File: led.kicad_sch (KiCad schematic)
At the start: 0 parts

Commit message: Add uC and PWM control for LEDs
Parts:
- added Q2, Q3, Q4, Q5, Q6, Q7: BSS214NW, Package_TO_SOT_SMD:SOT-323_SC-70, symbol Transistor_FET:BSS214NW
- added U10: ATtiny24-20P, Package_DIP:DIP-14_W7.62mm, symbol MCU_Microchip_ATtiny:ATtiny24-20P
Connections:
- new net: Q4.1 (G), U10.10 (PA3)
- new net: Q7.1 (G), U10.13 (AREF/PA0)
- new net: Q6.1 (G), U10.9 (PA4)
- new net: Q2.1 (G), U10.12 (PA1)
- new net: Q3.1 (G), U10.11 (PA2)
- new net: Q5.1 (G), U10.8 (PA5)
- new net GND: Q2.2 (S), Q3.2 (S), Q4.2 (S), Q5.2 (S), Q6.2 (S), Q7.2 (S), U10.14 (GND)
- new net LED_CH1: Q7.3 (D)
- new net LED_CH2: Q2.3 (D)
- new net LED_CH3: Q3.3 (D)
- new net LED_CH4: Q4.3 (D)
- new net LED_CH5: Q6.3 (D)
- new net LED_CH6: Q5.3 (D)
- new net VDD: U10.1 (VCC)

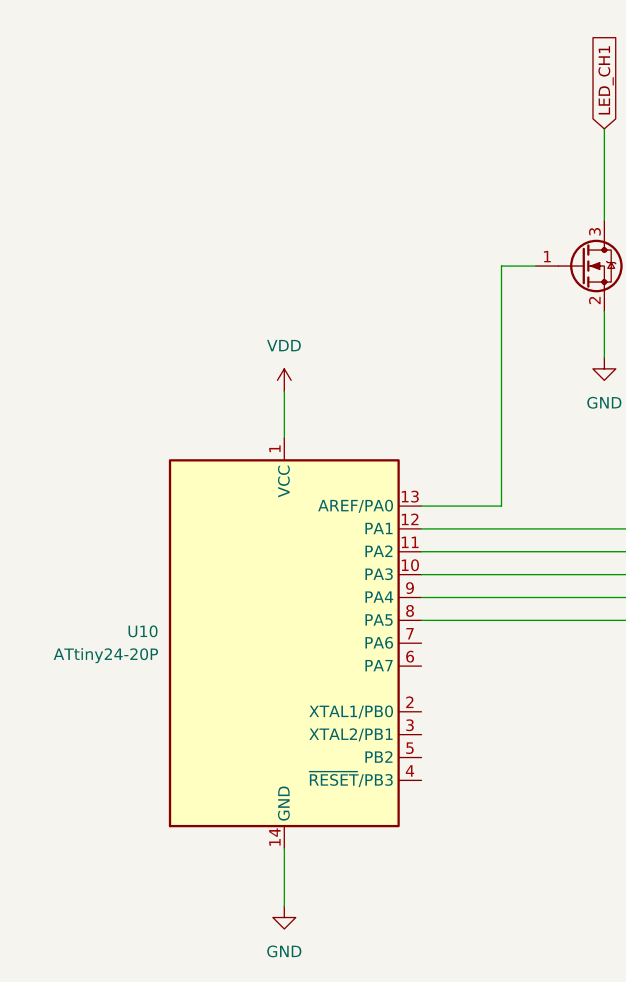
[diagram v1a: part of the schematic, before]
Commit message: Connect uC with LEDs
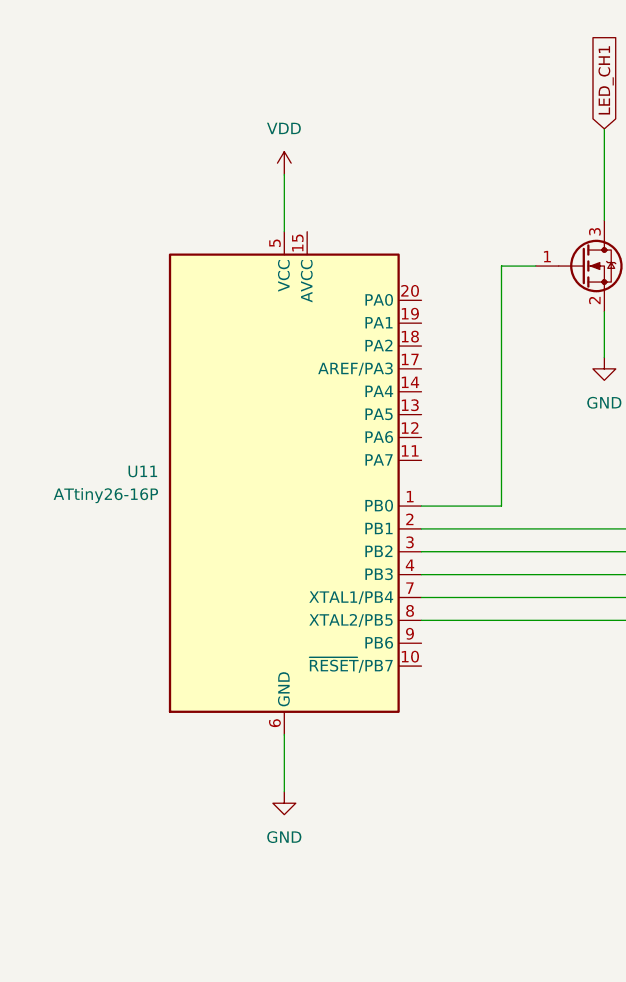
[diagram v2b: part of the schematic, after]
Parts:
- removed U10: ATtiny24-20P, Package_DIP:DIP-14_W7.62mm, symbol MCU_Microchip_ATtiny:ATtiny24-20P
- added U11: ATtiny26-16P, Package_DIP:DIP-20_W7.62mm, symbol MCU_Microchip_ATtiny:ATtiny26-16P
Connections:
- net GND: now also U11.16 (GND), U11.6 (GND)
- net VDD: now also U11.5 (VCC)
- net at Q4.1 (G): now also U11.4 (PB3)
- net at Q7.1 (G): now also U11.1 (PB0)
- net at Q6.1 (G): now also U11.7 (XTAL1/PB4)
- net at Q2.1 (G): now also U11.2 (PB1)
- net at Q3.1 (G): now also U11.3 (PB2)
- net at Q5.1 (G): now also U11.8 (XTAL2/PB5)
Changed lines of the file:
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@@
     (stroke (width 0) (type default))
   )
-  (wire (pts (xy 52.07 142.24) (xy 52.07 148.59))
+  (wire (pts (xy 52.07 129.54) (xy 52.07 135.89))
     (stroke (width 0) (type default))
   )
@@
     (stroke (width 0) (type default))
   )
+  (wire (pts (xy 52.07 73.66) (xy 52.07 67.31))
+    (stroke (width 0) (type default))
+  )
   (wire (pts (xy 215.9 82.55) (xy 215.9 87.63))
     (stroke (width 0) (type default))
@@
     (stroke (width 0) (type default))
   )
-  (wire (pts (xy 52.07 91.44) (xy 52.07 96.52))
-    (stroke (width 0) (type default))
-  )
   (wire (pts (xy 180.34 114.3) (xy 180.34 77.47))
     (stroke (width 0) (type default))
@@
     )
   )
-  (symbol (lib_id "power:VDD") (at 52.07 91.44 0) (unit 1)
-    (in_bom yes) (on_board yes) (dnp no) (fields_autoplaced)
-    (property "Reference" "#PWR033" (at 52.07 95.25 0)
-      (effects (font (size 1.27 1.27)) hide)
-    )
-    (property "Value" "VDD" (at 52.07 86.36 0)
-      (effects (font (size 1.27 1.27)))
-    )
-    (property "Footprint" "" (at 52.07 91.44 0)
-      (effects (font (size 1.27 1.27)) hide)
-    )
-    (property "Datasheet" "" (at 52.07 91.44 0)
+  (symbol (lib_id "power:VDD") (at 52.07 67.31 0) (unit 1)
+    (in_bom yes) (on_board yes) (dnp no) (fields_autoplaced)
+    (property "Reference" "#PWR033" (at 52.07 71.12 0)
+      (effects (font (size 1.27 1.27)) hide)
+    )
+    (property "Value" "VDD" (at 52.07 62.23 0)
+      (effects (font (size 1.27 1.27)))
+    )
+    (property "Footprint" "" (at 52.07 67.31 0)
+      (effects (font (size 1.27 1.27)) hide)
+    )
+    (property "Datasheet" "" (at 52.07 67.31 0)
       (effects (font (size 1.27 1.27)) hide)
     )
@@
     )
   )
+  (symbol (lib_id "MCU_Microchip_ATtiny:ATtiny26-16P") (at 52.07 101.6 0) (unit 1)
+    (in_bom yes) (on_board yes) (dnp no) (fields_autoplaced)
+    (property "Reference" "U11" (at 38.1 100.33 0)
+      (effects (font (size 1.27 1.27)) (justify right))
+    )
+    (property "Value" "ATtiny26-16P" (at 38.1 102.87 0)
+      (effects (font (size 1.27 1.27)) (justify right))
+    )
+    (property "Footprint" "Package_DIP:DIP-20_W7.62mm" (at 52.07 101.6 0)
+      (effects (font (size 1.27 1.27) italic) hide)
+    )
+    (property "Datasheet" "http://ww1.microchip.com/downloads/en/DeviceDoc/doc1477.pdf" (at 52.07 101.6 0)
+      (effects (font (size 1.27 1.27)) hide)
+    )
+    (pin "8")
+    (pin "20")
+    (pin "11")
+    (pin "18")
+    (pin "13")
+    (pin "15")
+    (pin "16")
+    (pin "1")
+    (pin "17")
+    (pin "10")
+    (pin "19")
+    (pin "7")
+    (pin "2")
+    (pin "5")
+    (pin "12")
+    (pin "4")
+    (pin "6")
+    (pin "14")
+    (pin "3")
+    (pin "9")
+    (instances
+      (project "aqua_driver"
+        (path "/13f34ed6-0d14-48e4-b5f6-041bf4b3feac/a0edc922-1405-4b8d-a73b-04ed23099c00"
+          (reference "U11") (unit 1)
+        )
+      )
+    )
+  )
   (symbol (lib_id "Transistor_FET:BSS214NW") (at 187.96 77.47 0) (unit 1)
     (in_bom yes) (on_board yes) (dnp no) (fields_autoplaced)
@@
     )
   )
-  (symbol (lib_id "MCU_Microchip_ATtiny:ATtiny24-20P") (at 52.07 119.38 0) (unit 1)
-    (in_bom yes) (on_board yes) (dnp no) (fields_autoplaced)
-    (property "Reference" "U10" (at 38.1 118.11 0)
-      (effects (font (size 1.27 1.27)) (justify right))
-    )
-    (property "Value" "ATtiny24-20P" (at 38.1 120.65 0)
-      (effects (font (size 1.27 1.27)) (justify right))
-    )
-    (property "Footprint" "Package_DIP:DIP-14_W7.62mm" (at 52.07 119.38 0)
-      (effects (font (size 1.27 1.27) italic) hide)
-    )
-    (property "Datasheet" "http://ww1.microchip.com/downloads/en/DeviceDoc/doc8006.pdf" (at 52.07 119.38 0)
-      (effects (font (size 1.27 1.27)) hide)
-    )
-    (pin "11")
-    (pin "12")
-    (pin "6")
-    (pin "8")
-    (pin "7")
-    (pin "5")
-    (pin "1")
-    (pin "9")
-    (pin "4")
-    (pin "2")
-    (pin "14")
-    (pin "13")
-    (pin "10")
-    (pin "3")
-    (instances
-      (project "aqua_driver"
-        (path "/13f34ed6-0d14-48e4-b5f6-041bf4b3feac/a0edc922-1405-4b8d-a73b-04ed23099c00"
-          (reference "U10") (unit 1)
-        )
-      )
-    )
-  )
   (symbol (lib_id "power:GND") (at 215.9 87.63 0) (unit 1)
     (in_bom yes) (on_board yes) (dnp no) (fields_autoplaced)
@@
     )
   )
-  (symbol (lib_id "power:GND") (at 52.07 148.59 0) (unit 1)
-    (in_bom yes) (on_board yes) (dnp no) (fields_autoplaced)
-    (property "Reference" "#PWR032" (at 52.07 154.94 0)
-      (effects (font (size 1.27 1.27)) hide)
-    )
-    (property "Value" "GND" (at 52.07 153.67 0)
-      (effects (font (size 1.27 1.27)))
-    )
-    (property "Footprint" "" (at 52.07 148.59 0)
-      (effects (font (size 1.27 1.27)) hide)
-    )
-    (property "Datasheet" "" (at 52.07 148.59 0)
-      (effects (font (size 1.27 1.27)) hide)
-    )
+  (symbol (lib_id "power:GND") (at 52.07 135.89 0) (unit 1)
+    (in_bom yes) (on_board yes) (dnp no) (fields_autoplaced)
+    (property "Reference" "#PWR032" (at 52.07 142.24 0)
+      (effects (font (size 1.27 1.27)) hide)
+    )
+    (property "Value" "GND" (at 52.07 140.97 0)
+      (effects (font (size 1.27 1.27)))
+    )
+    (property "Footprint" "" (at 52.07 135.89 0)
+      (effects (font (size 1.27 1.27)) hide)
+    )
+    (property "Datasheet" "" (at 52.07 135.89 0)
+      (effects (font (size 1.27 1.27)) hide)
+    )
